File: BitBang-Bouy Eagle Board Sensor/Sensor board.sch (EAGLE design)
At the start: 4 parts

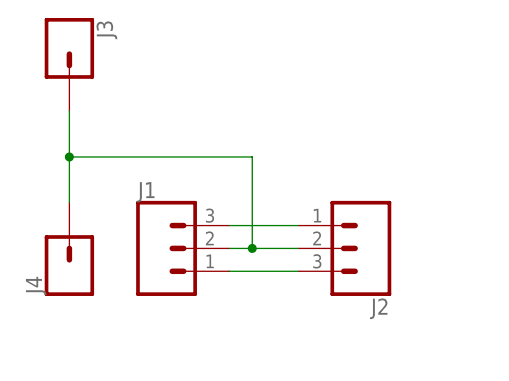
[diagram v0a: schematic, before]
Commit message: Trascient detector added
A trascient detector added in order to read mor accurately the hall sensor, it uses a registry ring and a window lecture
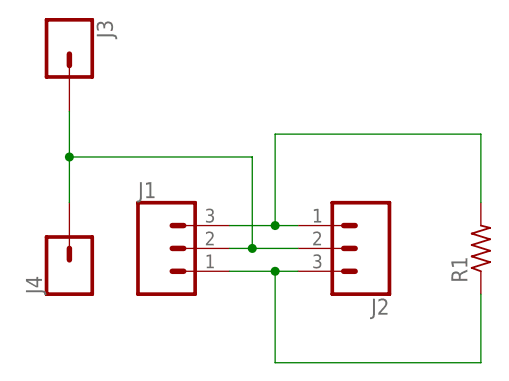
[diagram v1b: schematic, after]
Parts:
- added R1: (no value), rcl:R-US_0204/7
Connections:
- net N$1: now also R1.2
- net N$3: now also R1.1
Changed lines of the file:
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@@
 <?xml version="1.0" encoding="utf-8"?>
 <!DOCTYPE eagle SYSTEM "eagle.dtd">
-<eagle version="8.6.3">
+<eagle version="9.1.0">
 <drawing>
 <settings>
@@
 <part name="J3" library="SparkFun-Connectors" deviceset="CONN_01" device="SMTSO-256-ET-0.165DIA"/>
 <part name="J4" library="SparkFun-Connectors" deviceset="CONN_01" device="SMTSO-256-ET-0.165DIA"/>
+<part name="R1" library="rcl" library_urn="urn:adsk.eagle:library:334" deviceset="R-US_" device="0204/7" package3d_urn="urn:adsk.eagle:package:23498/1"/>
 </parts>
 <sheets>
@@
 <instance part="J3" gate="G$1" x="15.24" y="83.82" rot="R270"/>
 <instance part="J4" gate="G$1" x="15.24" y="58.42" rot="R90"/>
+<instance part="R1" gate="G$1" x="60.96" y="60.96" rot="R90"/>
 </instances>
 <busses>
@@
 <pinref part="J1" gate="J$1" pin="3"/>
 <pinref part="J2" gate="J$1" pin="1"/>
-<wire x1="33.02" y1="63.5" x2="40.64" y2="63.5" width="0.1524" layer="91"/>
+<wire x1="33.02" y1="63.5" x2="38.1" y2="63.5" width="0.1524" layer="91"/>
+<wire x1="38.1" y1="63.5" x2="40.64" y2="63.5" width="0.1524" layer="91"/>
+<wire x1="38.1" y1="63.5" x2="38.1" y2="73.66" width="0.1524" layer="91"/>
+<junction x="38.1" y="63.5"/>
+<pinref part="R1" gate="G$1" pin="2"/>
+<wire x1="38.1" y1="73.66" x2="60.96" y2="73.66" width="0.1524" layer="91"/>
+<wire x1="60.96" y1="73.66" x2="60.96" y2="66.04" width="0.1524" layer="91"/>
 </segment>
 </net>
@@
 <pinref part="J1" gate="J$1" pin="1"/>
 <pinref part="J2" gate="J$1" pin="3"/>
-<wire x1="33.02" y1="58.42" x2="40.64" y2="58.42" width="0.1524" layer="91"/>
+<wire x1="33.02" y1="58.42" x2="38.1" y2="58.42" width="0.1524" layer="91"/>
+<wire x1="38.1" y1="58.42" x2="40.64" y2="58.42" width="0.1524" layer="91"/>
+<wire x1="38.1" y1="58.42" x2="38.1" y2="48.26" width="0.1524" layer="91"/>
+<junction x="38.1" y="58.42"/>
+<pinref part="R1" gate="G$1" pin="1"/>
+<wire x1="38.1" y1="48.26" x2="60.96" y2="48.26" width="0.1524" layer="91"/>
+<wire x1="60.96" y1="48.26" x2="60.96" y2="55.88" width="0.1524" layer="91"/>
 </segment>
 </net>
@@
 </schematic>
 </drawing>
+<compatibility>
+<note version="8.2" severity="warning">
+Since Version 8.2, EAGLE supports online libraries. The ids
+of those online libraries will not be understood (or retained)
+with this version.
+</note>
+<note version="8.3" severity="warning">
+Since Version 8.3, EAGLE supports URNs for individual library
+assets (packages, symbols, and devices). The URNs of those assets
+will not be understood (or retained) with this version.
+</note>
+<note version="8.3" severity="warning">
+Since Version 8.3, EAGLE supports the association of 3D packages
+with devices in libraries, schematics, and board files. Those 3D
+packages will not be understood (or retained) with this version.
+</note>
+<note version="8.4" severity="warning">
+Since Version 8.4, EAGLE supports properties for SPICE simulation.
+Probes in schematics and SPICE mapping objects found in parts and library devices
+will not be understood with this version. Update EAGLE to the latest version
+for full support of SPICE simulation.
+</note>
+</compatibility>
 </eagle>
